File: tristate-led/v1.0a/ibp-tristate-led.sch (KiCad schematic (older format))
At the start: 34 parts, among them J1 PMOD

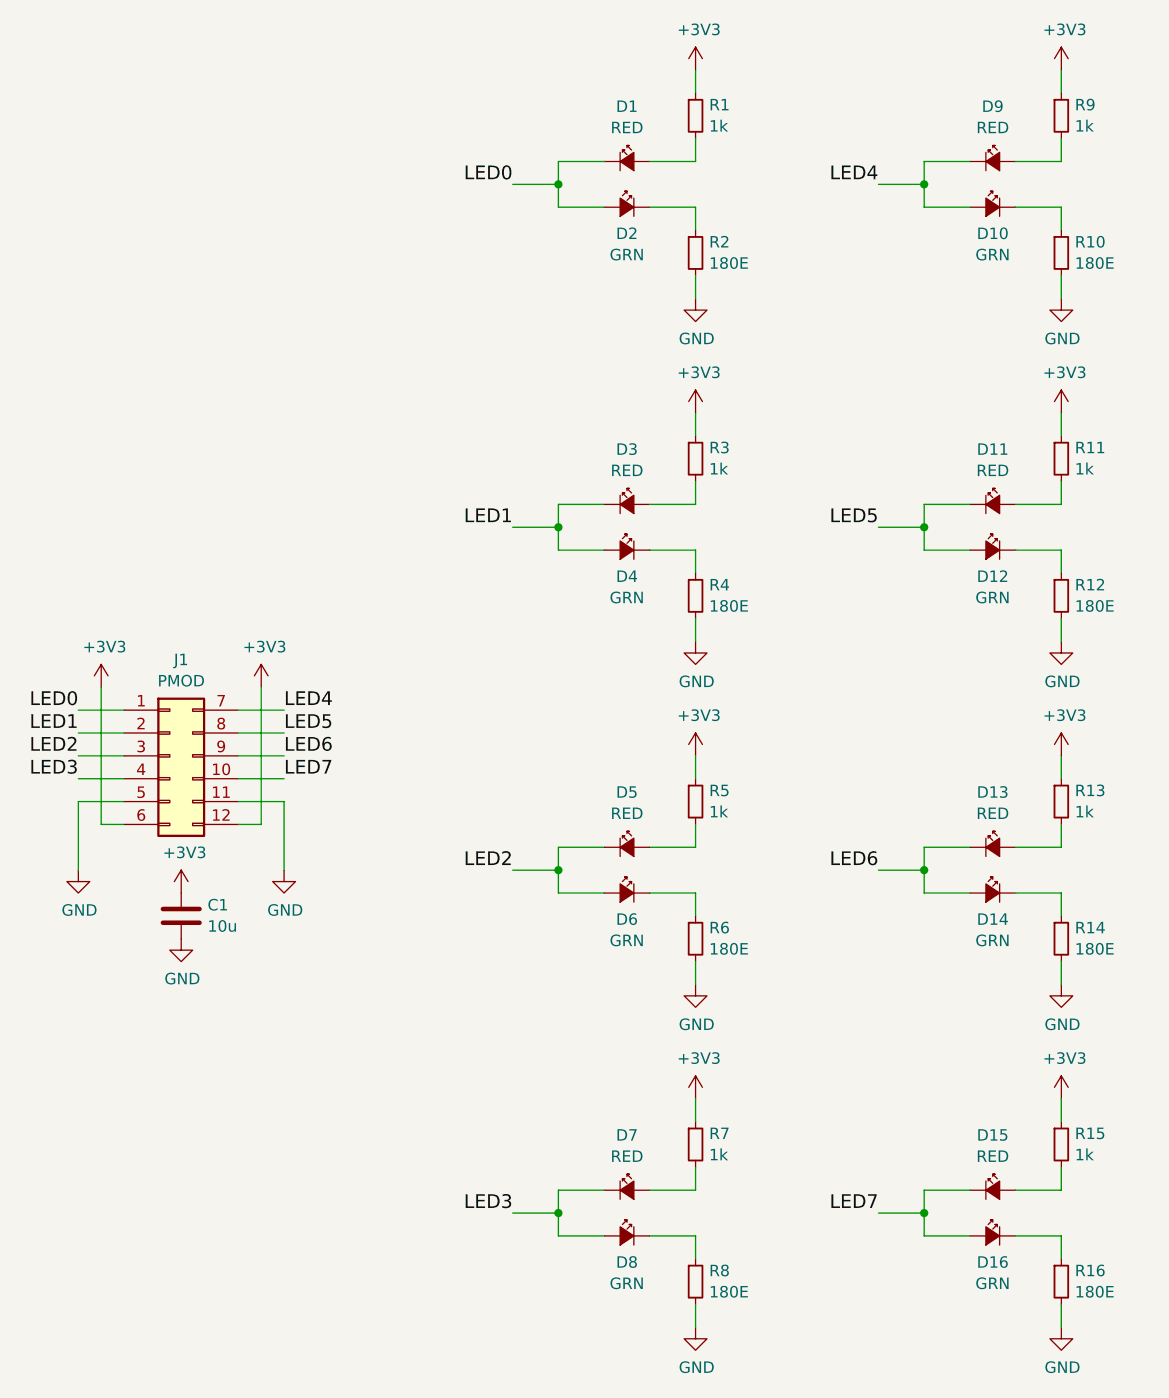
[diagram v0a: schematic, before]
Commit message: Cleaned up the schematic of the Tristate LED PMOD.
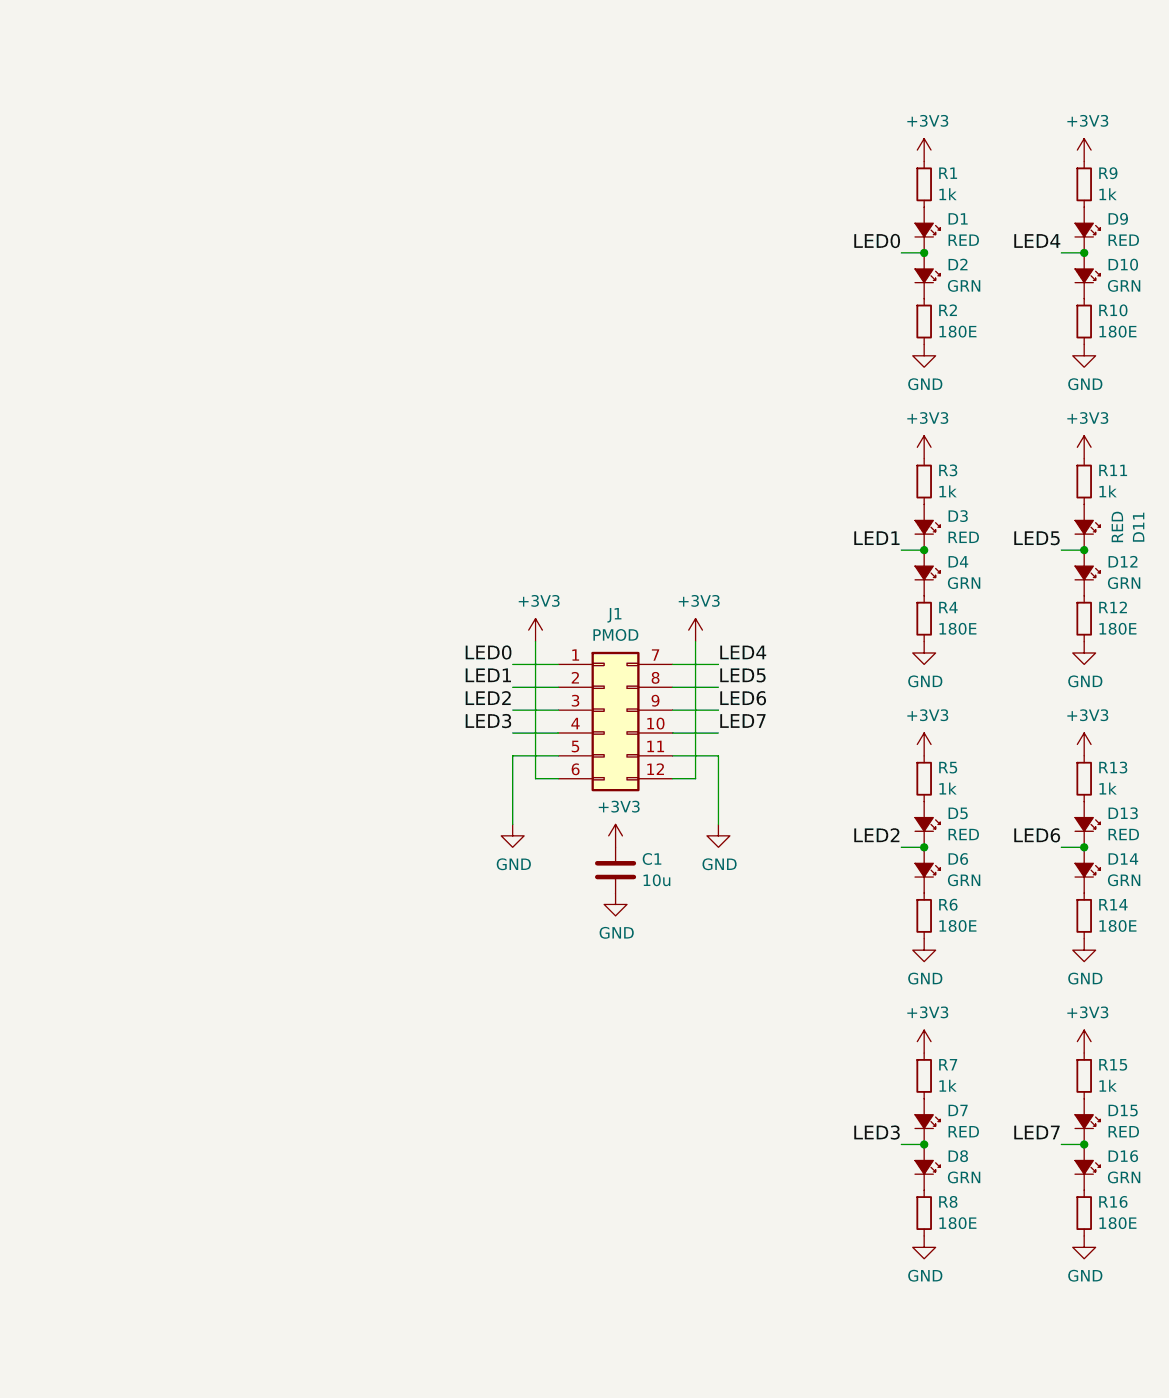
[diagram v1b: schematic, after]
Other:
- moved on the sheet: C1, D1, D10, D11, D12, D13, D14, D15, D16, D2, D3, D4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

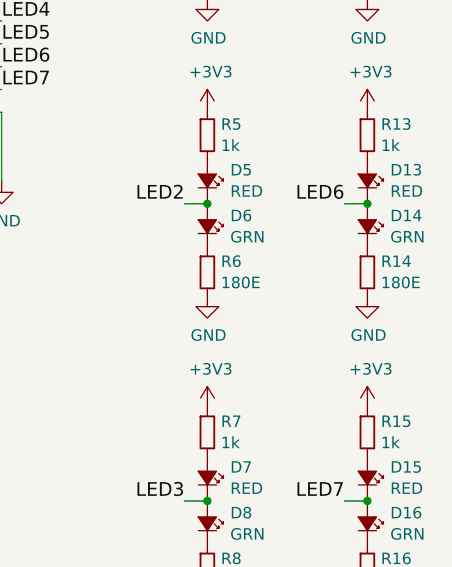
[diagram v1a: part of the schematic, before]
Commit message: Added pdf schematic exports to all projects plus minor fixes.
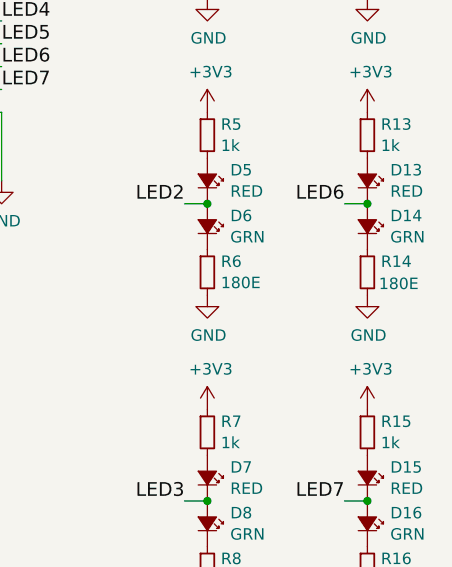
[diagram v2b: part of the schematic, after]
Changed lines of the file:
@@
 P 6800 4400
 F 0 "R14" H 6859 4447 50  0000 L CNN
-F 1 "180E" H 6859 4354 50  0000 L CNN
+F 1 "180E" H 6850 4350 50  0000 L CNN
 F 2 "pkl_dipol:R_0402" H 6800 4400 60  0001 C CNN
 F 3 "" H 6800 4400 60  0000 C CNN
